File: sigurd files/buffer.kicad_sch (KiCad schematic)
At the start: 2 parts, among them U7 LMV324AIDR

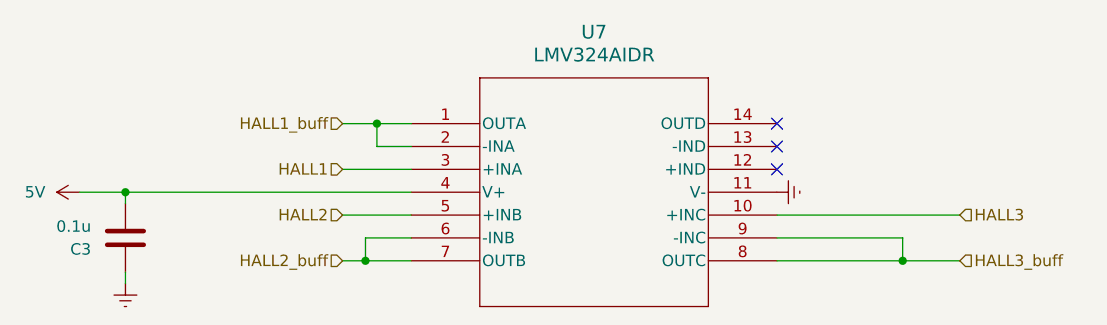
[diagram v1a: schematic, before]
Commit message: Everything but power traces routed
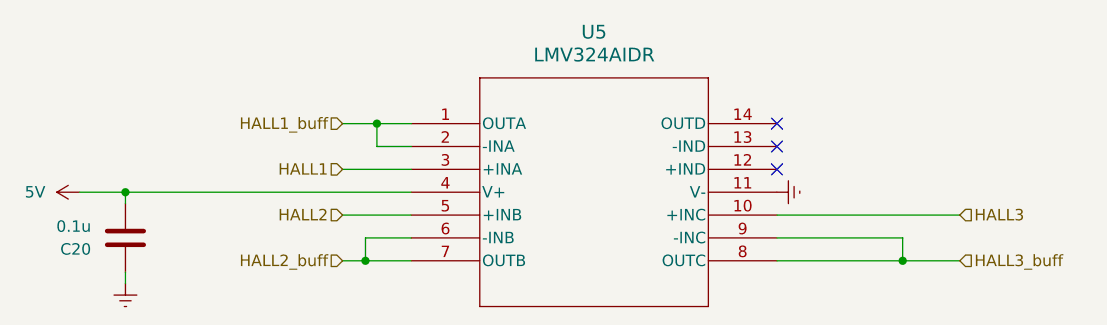
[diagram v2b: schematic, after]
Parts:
- renumbered C3 to C20, U7 to U5
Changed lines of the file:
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@@
 		(dnp no)
 		(fields_autoplaced yes)
-		(property "Reference" "#PWR033"
+		(property "Reference" "#PWR063"
 			(at 111.76 80.01 0)
 			(effects
@@
 			(project "SIGURD"
 				(path "/a4a592a3-08d1-41ec-9dda-18a75407e2f6/a5e08dc3-4335-44e4-be16-38fa9099f3c5"
-					(reference "#PWR033")
+					(reference "#PWR063")
 					(unit 1)
 				)
@@
 		(dnp no)
 		(fields_autoplaced yes)
-		(property "Reference" "U7"
+		(property "Reference" "U5"
 			(at 163.83 45.72 0)
 			(effects
@@
 			(project "SIGURD"
 				(path "/a4a592a3-08d1-41ec-9dda-18a75407e2f6/a5e08dc3-4335-44e4-be16-38fa9099f3c5"
-					(reference "U7")
+					(reference "U5")
 					(unit 1)
 				)
@@
 		(dnp no)
 		(fields_autoplaced yes)
-		(property "Reference" "#PWR044"
+		(property "Reference" "#PWR061"
 			(at 110.49 63.5 0)
 			(effects
@@
 			(project "SIGURD"
 				(path "/a4a592a3-08d1-41ec-9dda-18a75407e2f6/a5e08dc3-4335-44e4-be16-38fa9099f3c5"
-					(reference "#PWR044")
+					(reference "#PWR061")
 					(unit 1)
 				)
@@
 		(dnp no)
 		(fields_autoplaced yes)
-		(property "Reference" "#PWR047"
+		(property "Reference" "#PWR062"
 			(at 190.5 63.5 0)
 			(effects
@@
 			(project "SIGURD"
 				(path "/a4a592a3-08d1-41ec-9dda-18a75407e2f6/a5e08dc3-4335-44e4-be16-38fa9099f3c5"
-					(reference "#PWR047")
+					(reference "#PWR062")
 					(unit 1)
 				)
@@
 		(dnp no)
 		(fields_autoplaced yes)
-		(property "Reference" "C3"
+		(property "Reference" "C20"
 			(at 107.95 69.8501 0)
 			(effects
@@
 			(project "SIGURD"
 				(path "/a4a592a3-08d1-41ec-9dda-18a75407e2f6/a5e08dc3-4335-44e4-be16-38fa9099f3c5"
-					(reference "C3")
-					(unit 1)
-				)
+					(reference "C20")
+					(unit 1)
+				)
